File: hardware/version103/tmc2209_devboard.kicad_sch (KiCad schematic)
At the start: 41 parts, among them J1 Conn_01x02_Male, J2 Conn_01x03_Pin, J4 motor_conn, J5 motor_conn, J6 motor_conn, SW1 SW_Push, U1 TMC2209-LA

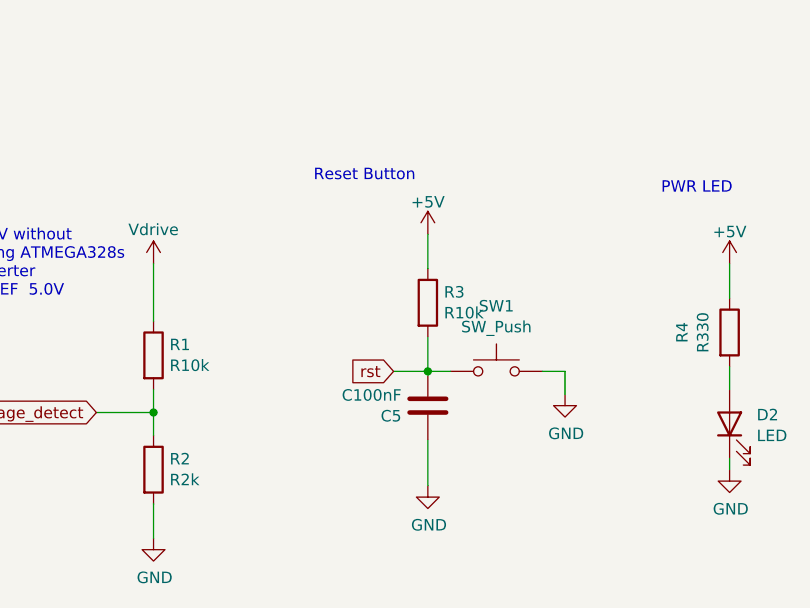
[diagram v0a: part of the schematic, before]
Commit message: changed motor power source connector and elec cap for lower nema17 placement. Added production files for 103
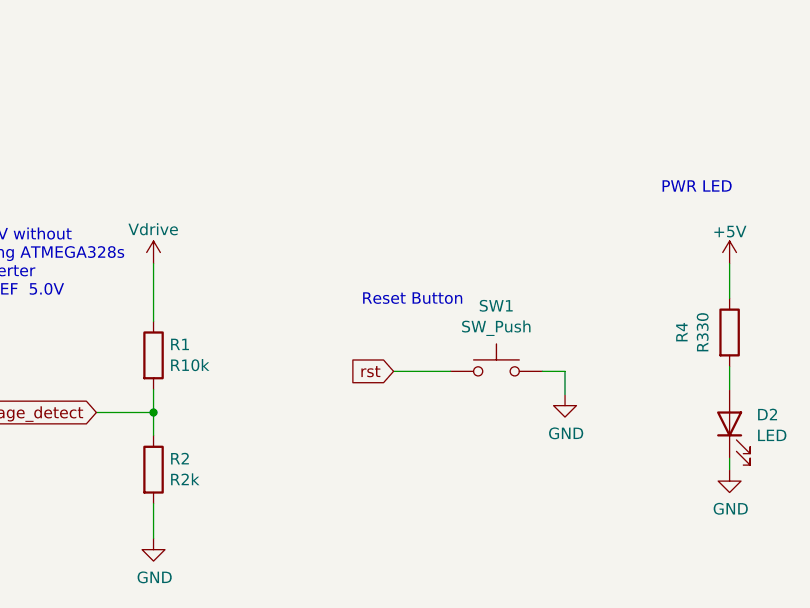
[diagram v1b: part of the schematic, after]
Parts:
- removed C5: C100nF, Capacitor_SMD:C_0805_2012Metric, symbol Device:C
- removed R3: R10k, Resistor_SMD:R_0805_2012Metric, symbol Device:R
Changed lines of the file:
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@@
   (junction (at 178.435 47.752) (diameter 0) (color 0 0 0 0)
   )
-  (junction (at 100.838 206.756) (diameter 0) (color 0 0 0 0)
-  )
   (junction (at 70.231 78.232) (diameter 0) (color 0 0 0 0)
   )
@@
     (stroke (width 0) (type default))
   )
-  (wire (pts (xy 100.838 202.946) (xy 100.838 206.756))
-    (stroke (width 0) (type default))
-  )
   (wire (pts (xy 212.09 216.408) (xy 212.09 224.028))
     (stroke (width 0) (type default))
@@
     (stroke (width 0) (type default))
   )
-  (wire (pts (xy 100.838 195.326) (xy 100.838 191.516))
-    (stroke (width 0) (type default))
-  )
-  (wire (pts (xy 97.028 206.756) (xy 100.838 206.756))
+  (wire (pts (xy 97.028 206.756) (xy 103.378 206.756))
     (stroke (width 0) (type default))
   )
@@
     (stroke (width 0) (type default))
   )
-  (wire (pts (xy 100.838 214.376) (xy 100.838 219.456))
-    (stroke (width 0) (type default))
-  )
   (wire (pts (xy 106.68 141.986) (xy 106.68 135.636))
     (stroke (width 0) (type default))
@@
   )
   (wire (pts (xy 64.008 211.328) (xy 70.358 211.328))
-    (stroke (width 0) (type default))
-  )
-  (wire (pts (xy 100.838 206.756) (xy 103.378 206.756))
     (stroke (width 0) (type default))
   )
@@
     (effects (font (size 1.27 1.27)) (justify left bottom))
   )
-  (text "Reset Button" (at 88.138 185.801 0)
+  (text "Reset Button" (at 93.472 199.644 0)
     (effects (font (size 1.27 1.27)) (justify left bottom))
   )
@@
     )
   )
-  (symbol (lib_id "power:+5V") (at 100.838 191.516 0) (unit 1)
-    (in_bom yes) (on_board yes) (dnp no) (fields_autoplaced)
-    (property "Reference" "#PWR011" (at 100.838 195.326 0)
-      (effects (font (size 1.27 1.27)) hide)
-    )
-    (property "Value" "+5V" (at 100.838 187.96 0)
-      (effects (font (size 1.27 1.27)))
-    )
-    (property "Footprint" "" (at 100.838 191.516 0)
-      (effects (font (size 1.27 1.27)) hide)
-    )
-    (property "Datasheet" "" (at 100.838 191.516 0)
-      (effects (font (size 1.27 1.27)) hide)
-    )
-    (pin "1")
-    (instances
-      (project "tmc2209_devboard"
-        (path "/269f19c3-6824-45a8-be29-fa58d70cbb42"
-          (reference "#PWR011") (unit 1)
-        )
-      )
-    )
-  )
   (symbol (lib_id "Device:R") (at 55.245 83.82 90) (unit 1)
     (in_bom yes) (on_board yes) (dnp no)
@@
     )
   )
-  (symbol (lib_id "power:GND") (at 100.838 219.456 0) (unit 1)
-    (in_bom yes) (on_board yes) (dnp no)
-    (property "Reference" "#PWR012" (at 100.838 225.806 0)
-      (effects (font (size 1.27 1.27)) hide)
-    )
-    (property "Value" "GND" (at 100.965 223.8502 0)
-      (effects (font (size 1.27 1.27)))
-    )
-    (property "Footprint" "" (at 100.838 219.456 0)
-      (effects (font (size 1.27 1.27)) hide)
-    )
-    (property "Datasheet" "" (at 100.838 219.456 0)
-      (effects (font (size 1.27 1.27)) hide)
-    )
-    (pin "1")
-    (instances
-      (project "tmc2209_devboard"
-        (path "/269f19c3-6824-45a8-be29-fa58d70cbb42"
-          (reference "#PWR012") (unit 1)
-        )
-      )
-    )
-  )
   (symbol (lib_id "power:GND") (at 134.366 217.678 0) (unit 1)
     (in_bom yes) (on_board yes) (dnp no)
@@
         (path "/269f19c3-6824-45a8-be29-fa58d70cbb42"
           (reference "#PWR019") (unit 1)
-        )
-      )
-    )
-  )
-  (symbol (lib_id "Device:R") (at 100.838 199.136 0) (unit 1)
-    (in_bom yes) (on_board yes) (dnp no)
-    (property "Reference" "R3" (at 102.616 197.9676 0)
-      (effects (font (size 1.27 1.27)) (justify left))
-    )
-    (property "Value" "R10k" (at 102.616 200.279 0)
-      (effects (font (size 1.27 1.27)) (justify left))
-    )
-    (property "Footprint" "Resistor_SMD:R_0805_2012Metric" (at 99.06 199.136 90)
-      (effects (font (size 1.27 1.27)) hide)
-    )
-    (property "Datasheet" "~" (at 100.838 199.136 0)
-      (effects (font (size 1.27 1.27)) hide)
-    )
-    (property "LCSC" "C340455" (at 100.838 199.136 0)
-      (effects (font (size 1.27 1.27)) hide)
-    )
-    (pin "1")
-    (pin "2")
-    (instances
-      (project "tmc2209_devboard"
-        (path "/269f19c3-6824-45a8-be29-fa58d70cbb42"
-          (reference "R3") (unit 1)
         )
       )
@@
         )
       )
-    )
-  )
-  (symbol (lib_id "Device:C") (at 100.838 210.566 180) (unit 1)
-    (in_bom yes) (on_board yes) (dnp no)
-    (property "Reference" "C5" (at 97.917 211.7344 0)
-      (effects (font (size 1.27 1.27)) (justify left))
-    )
-    (property "Value" "C100nF" (at 97.917 209.423 0)
-      (effects (font (size 1.27 1.27)) (justify left))
-    )
-    (property "Footprint" "Capacitor_SMD:C_0805_2012Metric" (at 99.8728 206.756 0)
-      (effects (font (size 1.27 1.27)) hide)
-    )
-    (property "Datasheet" "~" (at 100.838 210.566 0)
-      (effects (font (size 1.27 1.27)) hide)
-    )
-    (property "LCSC" "C49678" (at 100.838 210.566 0)
-      (effects (font (size 1.27 1.27)) hide)
-    )
-    (pin "1")
-    (pin "2")
-    (instances
-      (project "tmc2209_devboard"
-        (path "/269f19c3-6824-45a8-be29-fa58d70cbb42"
-          (reference "C5") (unit 1)
-        )
-      )

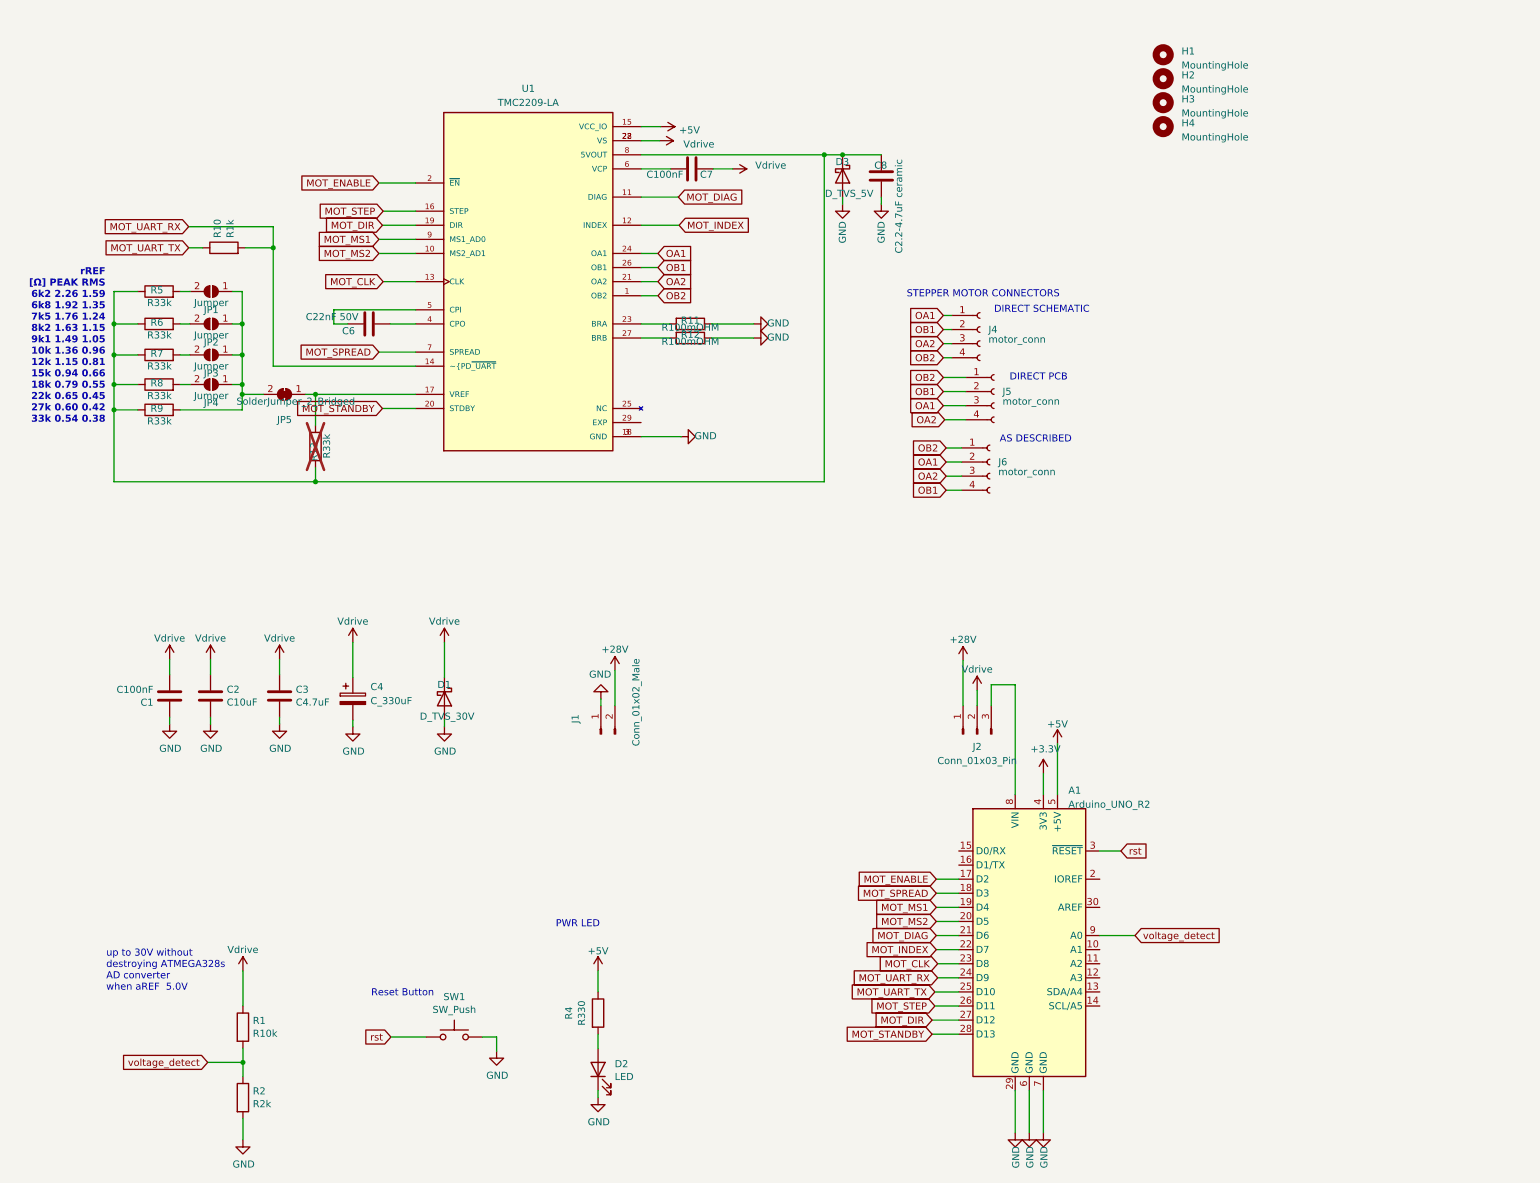
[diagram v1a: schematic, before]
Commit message: added gnd connection to motor mounts, added DNP for static PCB footprints
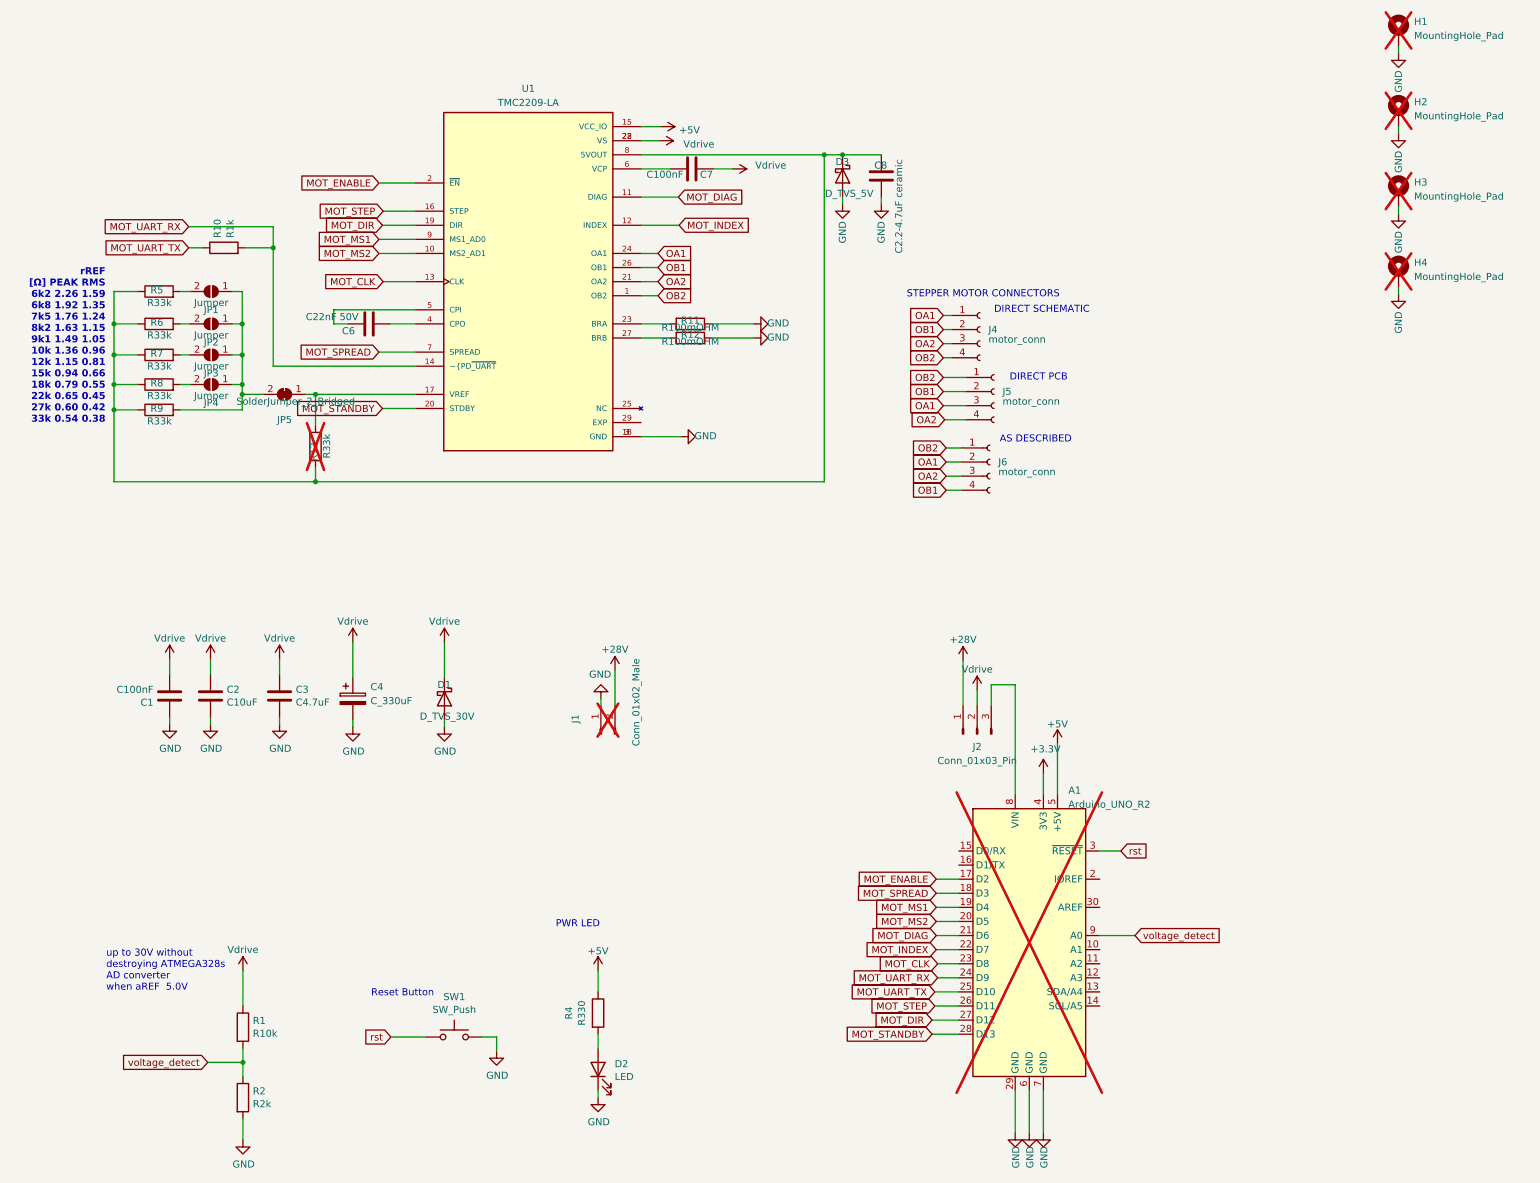
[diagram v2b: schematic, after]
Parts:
- removed H1, H2, H3, H4: MountingHole, MountingHole:MountingHole_3.2mm_M3_Pad, symbol Mechanical:MountingHole
- added H1, H2, H3, H4: MountingHole_Pad, MountingHole:MountingHole_3.2mm_M3_Pad_Via, symbol Mechanical:MountingHole_Pad
- A1, J1: now not fitted; now left out of the parts list
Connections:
- net GND: now also H1.1, H2.1, H3.1, H4.1

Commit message: minor
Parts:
- R1: LCSC C17415 -> C3016734
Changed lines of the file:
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@@
       (effects (font (size 1.27 1.27)) hide)
     )
-    (property "LCSC" "C17415" (at 70.358 204.978 0)
+    (property "LCSC" "C3016734" (at 70.358 204.978 0)
       (effects (font (size 1.27 1.27)) hide)
     )
